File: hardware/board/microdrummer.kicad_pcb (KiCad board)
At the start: 2 copper layers, 19 x 106.5 mm, 15 parts, among them J1 Thonk, J2 Thonk, J3 Thonk, SW1 SW_SPST, SW2 SW_SPST, U1 Teensy3.2

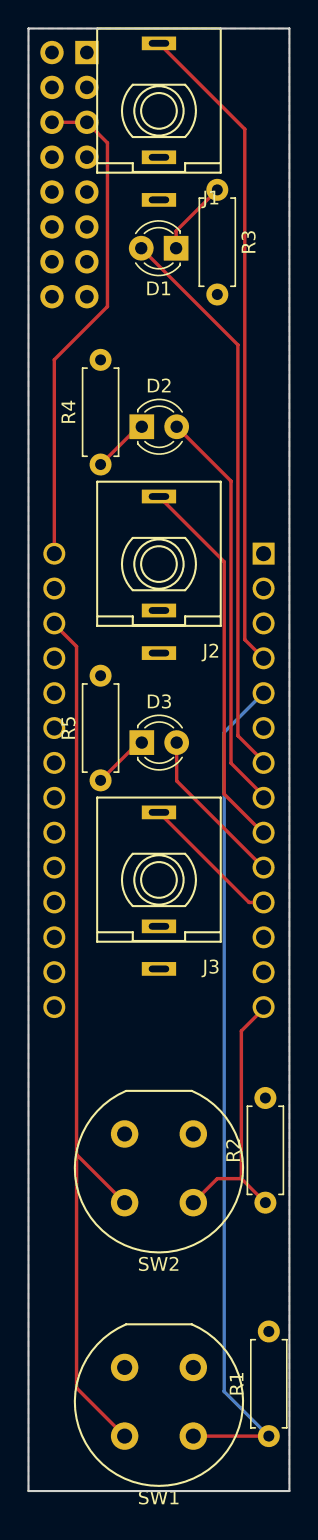
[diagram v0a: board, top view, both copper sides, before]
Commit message: layout updates, and moved pins around for 1-layer routing
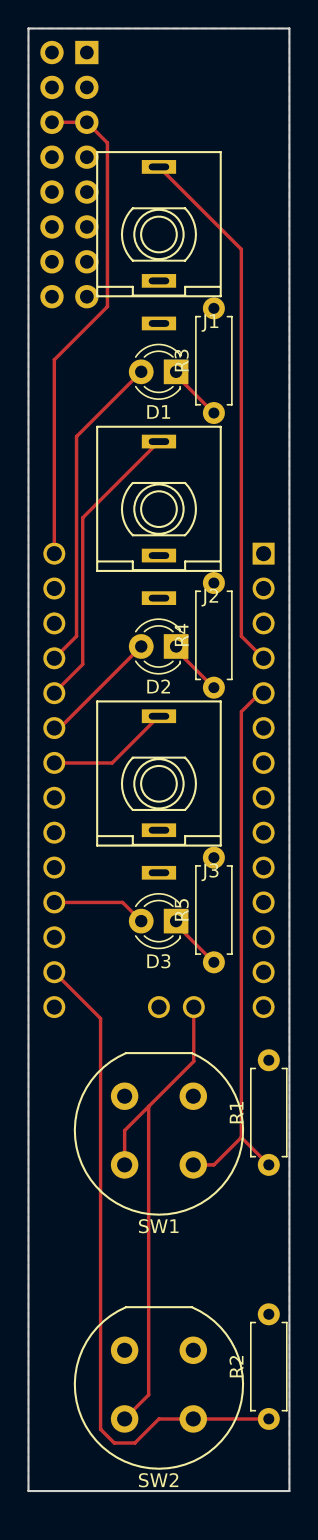
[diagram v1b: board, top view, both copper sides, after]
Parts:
- added G***: LOGO, drill_holes:cp_third_inch, B.Cu at (151.0, 42.5)
- U1: footprint teensy:Teensy30_31_32_LC -> teensy:Teensy30_31_32_LC_stdvgHeaders
- moved R1 19.8 mm to (154.5, 120.8)
- moved SW1 19.8 mm to (149.0, 120.8)
- moved R4 18.2 mm to (150.5, 86.0)
- moved R3 16.3 mm to (150.5, 66.0), turned to 90 degrees
- moved D2 16.2 mm to (147.8, 83.0), turned to 180 degrees
- moved R2 15.8 mm to (154.5, 139.2)
- moved SW2 15.8 mm to (149.0, 139.2)
- moved R5 15.6 mm to (150.5, 106.0)
- moved D3 13.2 mm to (147.8, 103.0), turned to 180 degrees
- moved D1 9.00 mm to (147.8, 63.0)
- moved J1 9.00 mm to (146.5, 53.0)
- moved J3 7.00 mm to (146.5, 93.0)
- moved J2 4.00 mm to (146.5, 73.0)
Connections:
- net Net-(J1-Pad3) renamed /SigIn
- net Net-(R1-Pad1) renamed /BtnIn
- D1 pad 2: Net-(D1-Pad2) -> /SigLed
- D2 pad 2: Net-(D2-Pad2) -> /GatLed
- D3 pad 2: Net-(D3-Pad2) -> /TrgLed
- J2 pad 3: Net-(J2-Pad3) -> /GatOut
- J3 pad 3: Net-(J3-Pad3) -> /TrgOut
- R2 pad 1: Net-(R2-Pad1) -> /BtnClr
- SW2 pad 1: Net-(R2-Pad1) -> /BtnClr
- U1 pad 10: Net-(D3-Pad2) -> (no net)
- U1 pad 11: Net-(J3-Pad3) -> (no net)
- U1 pad 14: Net-(R2-Pad1) -> (no net)
- U1 pad 21: (no net) -> /BtnClr
- U1 pad 23: (no net) -> /TrgLed
- U1 pad 27: (no net) -> /TrgOut
- U1 pad 28: (no net) -> /GatLed
- U1 pad 29: (no net) -> /GatOut
- U1 pad 30: (no net) -> /SigLed
- U1 pad 31: Net-(SW1-Pad2) -> (no net)
- U1 pad 7: Net-(D1-Pad2) -> (no net)
- U1 pad 8: Net-(D2-Pad2) -> (no net)
- U1 pad 9: Net-(J2-Pad3) -> (no net)
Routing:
- net /BtnClr: track 0.00 -> 48.1 mm
- net Net-(D1-Pad2): track 41.2 -> 0.00 mm
- net Net-(D2-Pad2): track 29.6 -> 0.00 mm
- net Net-(SW1-Pad2): track 66.3 -> 37.1 mm
- net Net-(J2-Pad3): track 27.7 -> 0.00 mm
- net /SigLed: track 0.00 -> 23.5 mm
- net /BtnIn: track 62.1 -> 40.4 mm
- net /GatOut: track 0.00 -> 21.5 mm
- net Net-(R2-Pad1): track 19.9 -> 0.00 mm
- net Net-(D3-Pad2): track 11.7 -> 0.00 mm
- net Net-(J3-Pad3): track 10.3 -> 0.00 mm
- net /TrgOut: track 0.00 -> 9.03 mm
- net /SigIn: track 47.9 -> 38.9 mm
- net /GatLed: track 0.00 -> 8.79 mm
- net /TrgLed: track 0.00 -> 6.89 mm
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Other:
- board text added: "BEATLOVERS"
